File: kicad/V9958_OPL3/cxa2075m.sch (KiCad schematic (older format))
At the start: 33 parts, among them P1 RED, P2 GREEN, P3 BLUE, P4 SYNC/C, U7 cxa2075M, X1 OSC, X3 S-VIDEO

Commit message: update
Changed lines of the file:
@@
 $EndComp
 $Comp
-L GND-RESCUE-v9958 #PWR27
+L GND-RESCUE-v9958 #PWR025
 U 1 1 5B035F00
 P 4450 3850
-F 0 "#PWR27" H 4450 3850 30  0001 C CNN
+F 0 "#PWR025" H 4450 3850 30  0001 C CNN
 F 1 "GND" H 4450 3780 30  0001 C CNN
 F 2 "" H 4450 3850 60  0000 C CNN
@@
 $EndComp
 $Comp
-L GND-RESCUE-v9958 #PWR29
+L GND-RESCUE-v9958 #PWR026
 U 1 1 5B035F0D
 P 5300 4300
-F 0 "#PWR29" H 5300 4300 30  0001 C CNN
+F 0 "#PWR026" H 5300 4300 30  0001 C CNN
 F 1 "GND" H 5300 4230 30  0001 C CNN
 F 2 "" H 5300 4300 60  0000 C CNN
@@
 $EndComp
 $Comp
-L GND-RESCUE-v9958 #PWR32
+L GND-RESCUE-v9958 #PWR027
 U 1 1 5B035F13
 P 7200 3300
-F 0 "#PWR32" H 7200 3300 30  0001 C CNN
+F 0 "#PWR027" H 7200 3300 30  0001 C CNN
 F 1 "GND" H 7200 3230 30  0001 C CNN
 F 2 "" H 7200 3300 60  0000 C CNN
@@
 $EndComp
 $Comp
-L VCC #PWR28
+L VCC #PWR028
 U 1 1 5B035F19
 P 4900 4600
-F 0 "#PWR28" H 4900 4700 30  0001 C CNN
+F 0 "#PWR028" H 4900 4700 30  0001 C CNN
 F 1 "VCC" H 4900 4700 30  0000 C CNN
 F 2 "" H 4900 4600 60  0000 C CNN
@@
 $EndComp
 $Comp
-L VCC #PWR37
+L VCC #PWR029
 U 1 1 5B035F1F
 P 7950 4000
-F 0 "#PWR37" H 7950 4100 30  0001 C CNN
+F 0 "#PWR029" H 7950 4100 30  0001 C CNN
 F 1 "VCC" H 7950 4100 30  0000 C CNN
 F 2 "" H 7950 4000 60  0000 C CNN
@@
 $EndComp
 $Comp
-L GND-RESCUE-v9958 #PWR39
+L GND-RESCUE-v9958 #PWR030
 U 1 1 5B035F87
 P 8200 4500
-F 0 "#PWR39" H 8200 4500 30  0001 C CNN
+F 0 "#PWR030" H 8200 4500 30  0001 C CNN
 F 1 "GND" H 8200 4430 30  0001 C CNN
 F 2 "" H 8200 4500 60  0000 C CNN
@@
 $EndComp
 $Comp
-L GND-RESCUE-v9958 #PWR30
+L GND-RESCUE-v9958 #PWR031
 U 1 1 5B035FB7
 P 5300 5100
-F 0 "#PWR30" H 5300 5100 30  0001 C CNN
+F 0 "#PWR031" H 5300 5100 30  0001 C CNN
 F 1 "GND" H 5300 5030 30  0001 C CNN
 F 2 "" H 5300 5100 60  0000 C CNN
@@
 $EndComp
 $Comp
-L GND-RESCUE-v9958 #PWR36
+L GND-RESCUE-v9958 #PWR032
 U 1 1 5B035FCB
 P 7900 4500
-F 0 "#PWR36" H 7900 4500 30  0001 C CNN
+F 0 "#PWR032" H 7900 4500 30  0001 C CNN
 F 1 "GND" H 7900 4430 30  0001 C CNN
 F 2 "" H 7900 4500 60  0000 C CNN
@@
 $EndComp
 $Comp
-L VCC #PWR25
+L VCC #PWR033
 U 1 1 5B035FD8
 P 2900 3800
-F 0 "#PWR25" H 2900 3900 30  0001 C CNN
+F 0 "#PWR033" H 2900 3900 30  0001 C CNN
 F 1 "VCC" H 2900 3900 30  0000 C CNN
 F 2 "" H 2900 3800 60  0000 C CNN
@@
 $EndComp
 $Comp
-L GND-RESCUE-v9958 #PWR26
+L GND-RESCUE-v9958 #PWR034
 U 1 1 5B035FDE
 P 2900 4650
-F 0 "#PWR26" H 2900 4650 30  0001 C CNN
+F 0 "#PWR034" H 2900 4650 30  0001 C CNN
 F 1 "GND" H 2900 4580 30  0001 C CNN
 F 2 "" H 2900 4650 60  0000 C CNN
@@
 $EndComp
 $Comp
-L GND-RESCUE-v9958 #PWR33
+L GND-RESCUE-v9958 #PWR035
 U 1 1 5B03600E
 P 7550 3150
-F 0 "#PWR33" H 7550 3150 30  0001 C CNN
+F 0 "#PWR035" H 7550 3150 30  0001 C CNN
 F 1 "GND" H 7550 3080 30  0001 C CNN
 F 2 "" H 7550 3150 60  0000 C CNN
@@
 $EndComp
 $Comp
-L GND-RESCUE-v9958 #PWR35
+L GND-RESCUE-v9958 #PWR036
 U 1 1 5B036014
 P 7800 3150
-F 0 "#PWR35" H 7800 3150 30  0001 C CNN
+F 0 "#PWR036" H 7800 3150 30  0001 C CNN
 F 1 "GND" H 7800 3080 30  0001 C CNN
 F 2 "" H 7800 3150 60  0000 C CNN
@@
 $EndComp
 $Comp
-L GND-RESCUE-v9958 #PWR38
+L GND-RESCUE-v9958 #PWR037
 U 1 1 5B03601A
 P 8050 3150
-F 0 "#PWR38" H 8050 3150 30  0001 C CNN
+F 0 "#PWR037" H 8050 3150 30  0001 C CNN
 F 1 "GND" H 8050 3080 30  0001 C CNN
 F 2 "" H 8050 3150 60  0000 C CNN
@@
 $EndComp
 $Comp
-L GND-RESCUE-v9958 #PWR41
+L GND-RESCUE-v9958 #PWR038
 U 1 1 5B036020
 P 8300 3150
-F 0 "#PWR41" H 8300 3150 30  0001 C CNN
+F 0 "#PWR038" H 8300 3150 30  0001 C CNN
 F 1 "GND" H 8300 3080 30  0001 C CNN
 F 2 "" H 8300 3150 60  0000 C CNN
@@
 $EndComp
 Wire Wire Line
-	3750 3050 5050 3050
+	3450 3050 5050 3050
 Wire Wire Line
 	4300 3050 4300 3250
@@
 Connection ~ 4300 3050
 Wire Wire Line
-	3750 2950 5250 2950
+	3450 2950 5250 2950
 Connection ~ 4450 2950
 Wire Wire Line
-	3750 2850 4850 2850
+	3450 2850 4850 2850
 Connection ~ 4600 2850
 Wire Wire Line
 	5050 3050 5050 3100
 Wire Wire Line
-	3750 3150 4700 3150
+	3450 3150 4700 3150
 Wire Wire Line
 	4700 3150 4700 4400
@@
 Wire Wire Line
 	4850 2850 4850 3100
-Wire Wire Line
-	3450 2850 3750 2850
-Wire Wire Line
-	3450 2950 3750 2950
-Wire Wire Line
-	3450 3050 3750 3050
-Wire Wire Line
-	3450 3150 3750 3150
 Text HLabel 3450 2850 0    60   Input ~ 0
 RGB_B
@@
 $EndComp
 $Comp
-L GND-RESCUE-v9958 #PWR31
+L GND-RESCUE-v9958 #PWR039
 U 1 1 5B038CCB
 P 6900 5850
-F 0 "#PWR31" H 6900 5850 30  0001 C CNN
+F 0 "#PWR039" H 6900 5850 30  0001 C CNN
 F 1 "GND" H 6900 5780 30  0001 C CNN
 F 2 "" H 6900 5850 60  0000 C CNN
@@
 $EndComp
 $Comp
-L GND-RESCUE-v9958 #PWR40
+L GND-RESCUE-v9958 #PWR040
 U 1 1 5B038CD1
 P 8200 5850
-F 0 "#PWR40" H 8200 5850 30  0001 C CNN
+F 0 "#PWR040" H 8200 5850 30  0001 C CNN
 F 1 "GND" H 8200 5780 30  0001 C CNN
 F 2 "" H 8200 5850 60  0000 C CNN
@@
 	7050 6050 7050 6250
 Wire Wire Line
-	7050 6250 7550 6250
-Wire Wire Line
-	7550 6250 8050 6250
+	7050 6250 8050 6250
 Wire Wire Line
 	8050 6250 8050 6050
 Connection ~ 7550 6250
 $Comp
-L GND-RESCUE-v9958 #PWR34
+L GND-RESCUE-v9958 #PWR041
 U 1 1 5B038CE4
 P 7550 6350
-F 0 "#PWR34" H 7550 6350 30  0001 C CNN
+F 0 "#PWR041" H 7550 6350 30  0001 C CNN
 F 1 "GND" H 7550 6280 30  0001 C CNN
 F 2 "" H 7550 6350 60  0000 C CNN

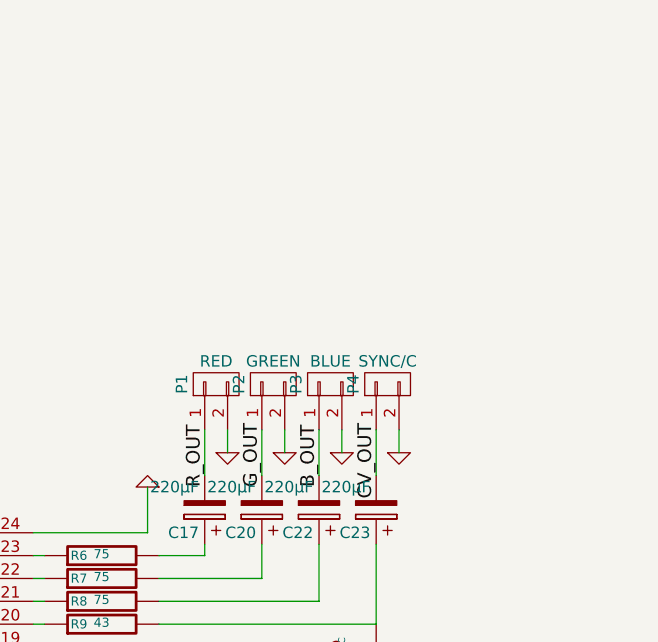
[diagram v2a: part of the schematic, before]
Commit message: dsub9-connector for RGB, pinout like 1084S D2
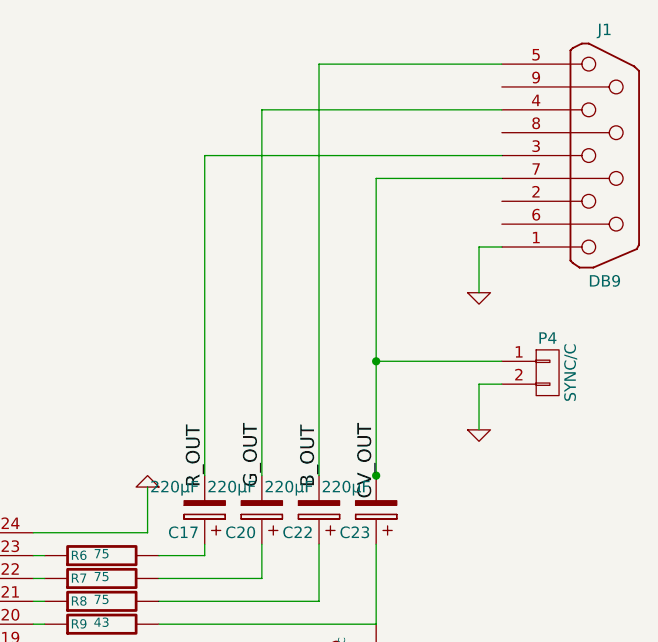
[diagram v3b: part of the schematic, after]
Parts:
- removed P1: RED, w_conn_av:rca_black, symbol CONN_01X02
- removed P2: GREEN, w_conn_av:rca_black, symbol CONN_01X02
- removed P3: BLUE, w_conn_av:rca_black, symbol CONN_01X02
- added J1: DB9, Connect:DB9FC, symbol DB9
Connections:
- net GND: now also J1.1
- net at C17.2: now also J1.3
- net at C20.2: now also J1.4
- net at C22.2: now also J1.5
- net at C23.2, P4.1 (P1): now also J1.7 (P7)
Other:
- moved on the sheet: P4
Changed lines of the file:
@@
 LIBS:yamaha_opl
 LIBS:rc4136
+LIBS:audio
 LIBS:v9958-cache
 EELAYER 25 0
@@
 Y_OUT
 $Comp
-L CONN_01X02 P1
-U 1 1 5B035FF2
-P 7500 2850
-F 0 "P1" H 7500 3000 50  0000 C CNN
-F 1 "RED" V 7600 2850 50  0000 C CNN
-F 2 "w_conn_av:rca_black" H 7500 2850 50  0001 C CNN
-F 3 "" H 7500 2850 50  0000 C CNN
-	1    7500 2850
-	0    -1   -1   0
-$EndComp
-$Comp
-L CONN_01X02 P2
-U 1 1 5B035FF9
-P 7750 2850
-F 0 "P2" H 7750 3000 50  0000 C CNN
-F 1 "GREEN" V 7850 2850 50  0000 C CNN
-F 2 "w_conn_av:rca_black" H 7750 2850 50  0001 C CNN
-F 3 "" H 7750 2850 50  0000 C CNN
-	1    7750 2850
-	0    -1   -1   0
-$EndComp
-$Comp
-L CONN_01X02 P3
-U 1 1 5B036000
-P 8000 2850
-F 0 "P3" H 8000 3000 50  0000 C CNN
-F 1 "BLUE" V 8100 2850 50  0000 C CNN
-F 2 "w_conn_av:rca_black" H 8000 2850 50  0001 C CNN
-F 3 "" H 8000 2850 50  0000 C CNN
-	1    8000 2850
-	0    -1   -1   0
-$EndComp
-$Comp
 L CONN_01X02 P4
 U 1 1 5B036007
-P 8250 2850
-F 0 "P4" H 8250 3000 50  0000 C CNN
-F 1 "SYNC/C" V 8350 2850 50  0000 C CNN
-F 2 "w_conn_av:rca_black" H 8250 2850 50  0001 C CNN
-F 3 "" H 8250 2850 50  0000 C CNN
-	1    8250 2850
-	0    -1   -1   0
+P 8950 2800
+F 0 "P4" H 8950 2950 50  0000 C CNN
+F 1 "SYNC/C" V 9050 2800 50  0000 C CNN
+F 2 "w_conn_av:rca_black" H 8950 2800 50  0001 C CNN
+F 3 "" H 8950 2800 50  0000 C CNN
+	1    8950 2800
+	1    0    0    -1
 $EndComp
 $Comp
 L GND-RESCUE-v9958 #PWR035
-U 1 1 5B03600E
-P 7550 3150
-F 0 "#PWR035" H 7550 3150 30  0001 C CNN
-F 1 "GND" H 7550 3080 30  0001 C CNN
-F 2 "" H 7550 3150 60  0000 C CNN
-F 3 "" H 7550 3150 60  0000 C CNN
-	1    7550 3150
-	1    0    0    -1
-$EndComp
-$Comp
-L GND-RESCUE-v9958 #PWR036
-U 1 1 5B036014
-P 7800 3150
-F 0 "#PWR036" H 7800 3150 30  0001 C CNN
-F 1 "GND" H 7800 3080 30  0001 C CNN
-F 2 "" H 7800 3150 60  0000 C CNN
-F 3 "" H 7800 3150 60  0000 C CNN
-	1    7800 3150
-	1    0    0    -1
-$EndComp
-$Comp
-L GND-RESCUE-v9958 #PWR037
-U 1 1 5B03601A
-P 8050 3150
-F 0 "#PWR037" H 8050 3150 30  0001 C CNN
-F 1 "GND" H 8050 3080 30  0001 C CNN
-F 2 "" H 8050 3150 60  0000 C CNN
-F 3 "" H 8050 3150 60  0000 C CNN
-	1    8050 3150
-	1    0    0    -1
-$EndComp
-$Comp
-L GND-RESCUE-v9958 #PWR038
 U 1 1 5B036020
-P 8300 3150
-F 0 "#PWR038" H 8300 3150 30  0001 C CNN
-F 1 "GND" H 8300 3080 30  0001 C CNN
-F 2 "" H 8300 3150 60  0000 C CNN
-F 3 "" H 8300 3150 60  0000 C CNN
-	1    8300 3150
+P 8650 3050
+F 0 "#PWR035" H 8650 3050 30  0001 C CNN
+F 1 "GND" H 8650 2980 30  0001 C CNN
+F 2 "" H 8650 3050 60  0000 C CNN
+F 3 "" H 8650 3050 60  0000 C CNN
+	1    8650 3050
 	1    0    0    -1
 $EndComp
@@
 	4800 4400 4700 4400
 Wire Wire Line
-	7450 3250 7450 3050
-Wire Wire Line
-	7700 3250 7700 3050
-Wire Wire Line
-	7950 3250 7950 3050
-Wire Wire Line
-	8200 3250 8200 3050
+	7450 1850 7450 3250
+Wire Wire Line
+	7700 1650 7700 3250
+Wire Wire Line
+	7950 1450 7950 3250
 Wire Wire Line
 	7550 4750 7550 5000
 Wire Wire Line
 	7300 4750 7300 5000
-Wire Wire Line
-	7550 3050 7550 3150
-Wire Wire Line
-	7800 3050 7800 3150
-Wire Wire Line
-	8050 3050 8050 3150
-Wire Wire Line
-	8300 3050 8300 3150
 NoConn ~ 5400 4200
 Wire Wire Line
@@
 $EndComp
 $Comp
-L GND-RESCUE-v9958 #PWR039
+L GND-RESCUE-v9958 #PWR036
 U 1 1 5B038CCB
 P 6900 5850
-F 0 "#PWR039" H 6900 5850 30  0001 C CNN
+F 0 "#PWR036" H 6900 5850 30  0001 C CNN
 F 1 "GND" H 6900 5780 30  0001 C CNN
 F 2 "" H 6900 5850 60  0000 C CNN
@@
 $EndComp
 $Comp
-L GND-RESCUE-v9958 #PWR040
+L GND-RESCUE-v9958 #PWR037
 U 1 1 5B038CD1
 P 8200 5850
-F 0 "#PWR040" H 8200 5850 30  0001 C CNN
+F 0 "#PWR037" H 8200 5850 30  0001 C CNN
 F 1 "GND" H 8200 5780 30  0001 C CNN
 F 2 "" H 8200 5850 60  0000 C CNN
@@
 Connection ~ 7550 6250
 $Comp
-L GND-RESCUE-v9958 #PWR041
+L GND-RESCUE-v9958 #PWR038
 U 1 1 5B038CE4
 P 7550 6350
-F 0 "#PWR041" H 7550 6350 30  0001 C CNN
+F 0 "#PWR038" H 7550 6350 30  0001 C CNN
 F 1 "GND" H 7550 6280 30  0001 C CNN
 F 2 "" H 7550 6350 60  0000 C CNN
@@
 Wire Wire Line
 	7550 6250 7550 6350
+$Comp
+L DB9 J1
+U 1 1 5B2FF0C6
+P 9200 1850
+F 0 "J1" H 9200 2400 50  0000 C CNN
+F 1 "DB9" H 9200 1300 50  0000 C CNN
+F 2 "Connect:DB9FC" H 9200 1850 50  0001 C CNN
+F 3 "" H 9200 1850 50  0000 C CNN
+	1    9200 1850
+	1    0    0    -1
+$EndComp
+Wire Wire Line
+	8750 1850 7450 1850
+Wire Wire Line
+	8750 1650 7700 1650
+Wire Wire Line
+	8750 1450 7950 1450
+Wire Wire Line
+	7950 3050 7950 3050
+$Comp
+L GND-RESCUE-v9958 #PWR039
+U 1 1 5B2FF2BC
+P 8650 2450
+F 0 "#PWR039" H 8650 2450 30  0001 C CNN
+F 1 "GND" H 8650 2380 30  0001 C CNN
+F 2 "" H 8650 2450 60  0000 C CNN
+F 3 "" H 8650 2450 60  0000 C CNN
+	1    8650 2450
+	1    0    0    -1
+$EndComp
+Wire Wire Line
+	8750 2250 8650 2250
+Wire Wire Line
+	8650 2250 8650 2450
+Wire Wire Line
+	8750 1950 8200 1950
+Wire Wire Line
+	8200 1950 8200 3250
+Connection ~ 8200 3250
+Wire Wire Line
+	8750 2850 8650 2850
+Wire Wire Line
+	8650 2850 8650 3050
+Wire Wire Line
+	8750 2750 8200 2750
+Connection ~ 8200 2750
 $EndSCHEMATC
